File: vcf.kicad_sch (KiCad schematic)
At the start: 49 parts, among them J6 Conn_01x11_Pin, Q4 BC307, U19 Opamp_Dual, U24 LM13700, U25 LM13700

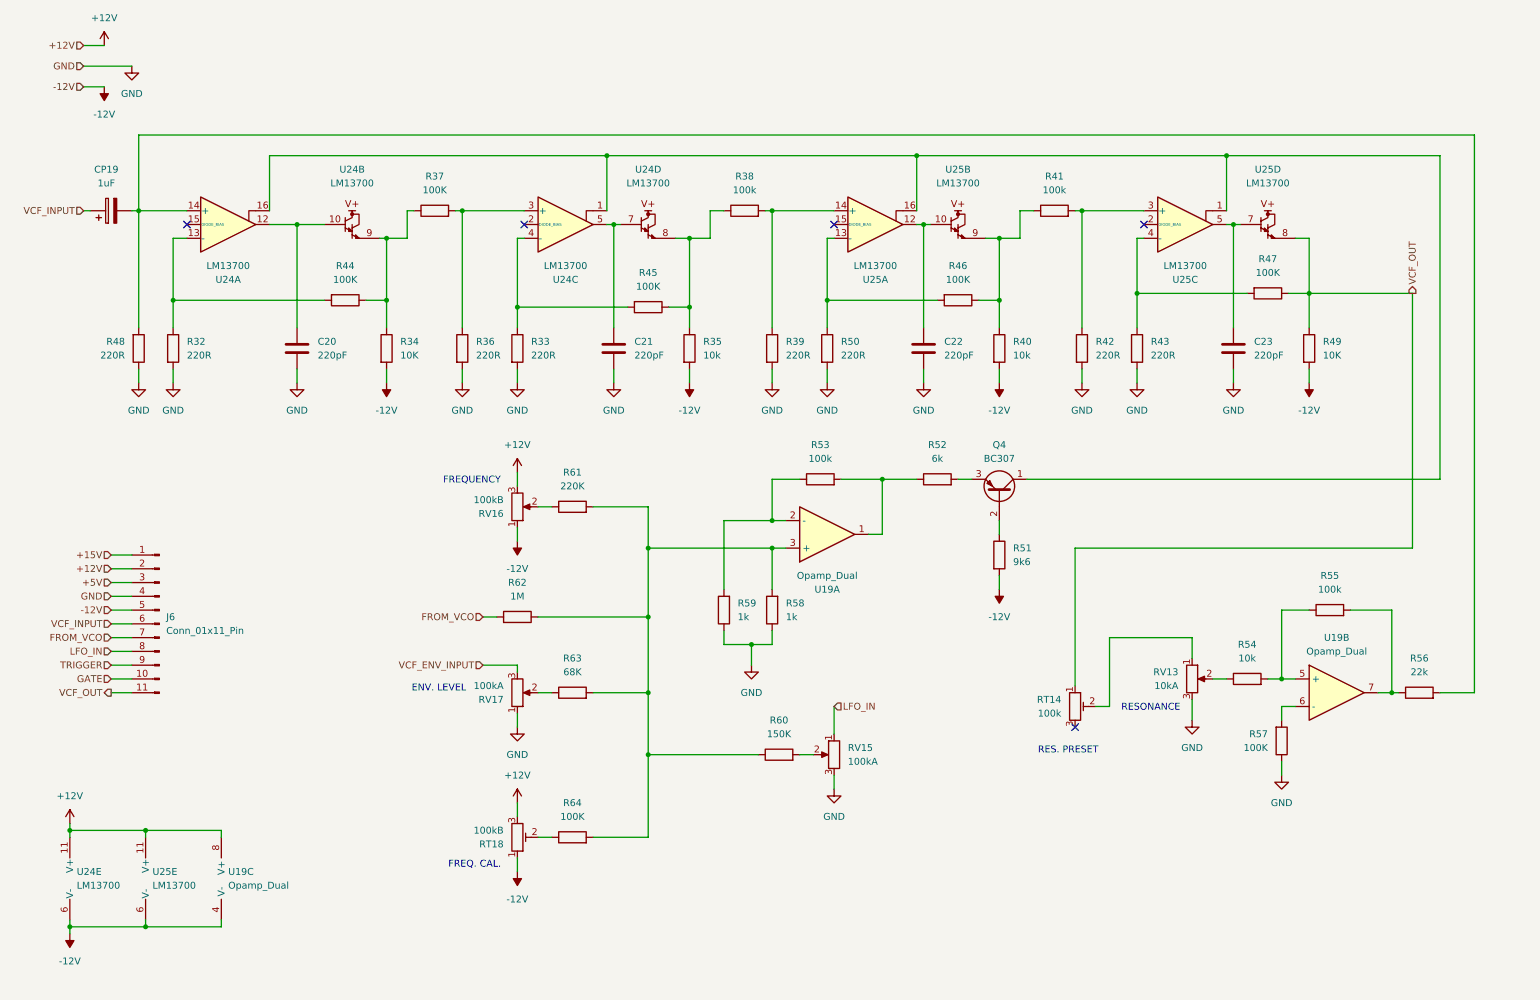
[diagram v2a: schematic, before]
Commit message: VCF components are in position (but PCB size is wrong)
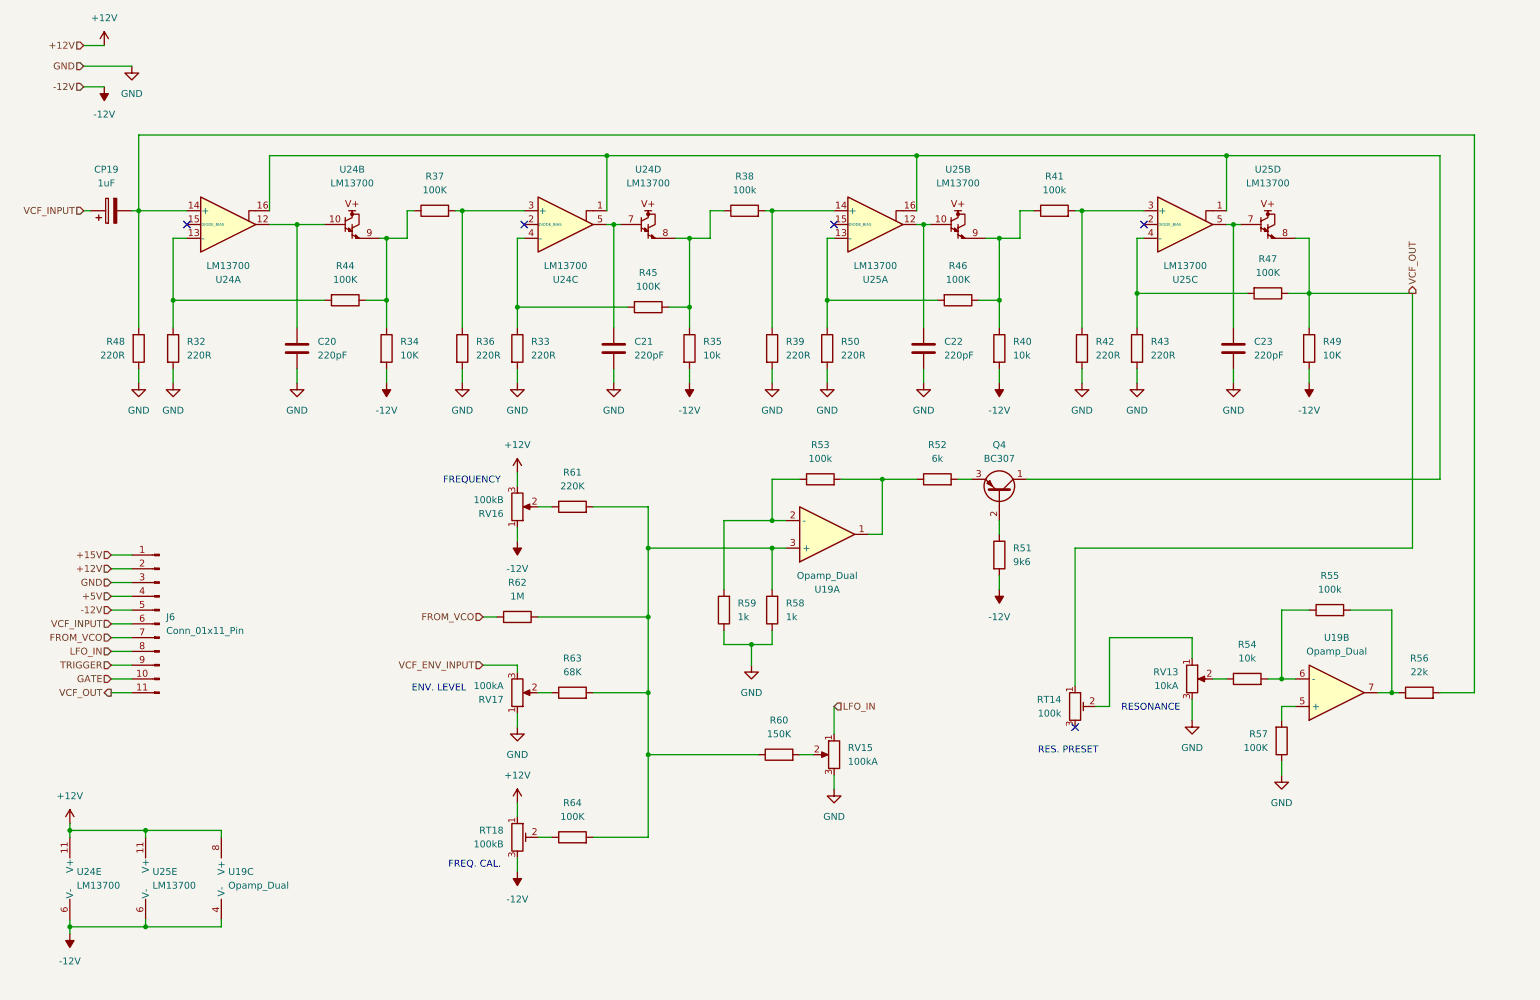
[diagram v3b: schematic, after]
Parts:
- Q4: footprint Package_TO_SOT_THT:TO-92_Inline -> Package_TO_SOT_THT:TO-92_Inline_Wide
- R32, R33, R34, R35, R36, R37, R38, R39, R40, R41, R42, R43, R44, R45, R46, R47, R48, R49, R50, R51, R52, R53, R54, R55, R56, R57, R58, R59, R60, R61, R62, R63, R64: footprint Resistor_THT:R_Axial_DIN0204_L3.6mm_D1.6mm_P7.62mm_Horizontal -> Resistor_THT:R_Axial_DIN0207_L6.3mm_D2.5mm_P15.24mm_Horizontal
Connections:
- net +12V: now also RT18.1; no longer RT18.3
- net +5V: now also J6.4 (Pin_4); no longer J6.3 (Pin_3)
- net -12V: now also RT18.3; no longer RT18.1
- net GND: now also J6.3 (Pin_3); no longer J6.4 (Pin_4)
- net at R54.2, R55.1: now also U19.6 (-); no longer U19.5 (+)
- net at R57.2: now also U19.5 (+); no longer U19.6 (-)
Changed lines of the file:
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@@
 	(hierarchical_label "GND"
 		(shape input)
-		(at 29.21 124.46 180)
+		(at 29.21 121.92 180)
 		(effects
 			(font
@@
 	(hierarchical_label "+5V"
 		(shape input)
-		(at 29.21 121.92 180)
+		(at 29.21 124.46 180)
 		(effects
 			(font
@@
 			)
 		)
-		(property "Footprint" "Resistor_THT:R_Axial_DIN0204_L3.6mm_D1.6mm_P7.62mm_Horizontal"
+		(property "Footprint" "Resistor_THT:R_Axial_DIN0207_L6.3mm_D2.5mm_P15.24mm_Horizontal"
 			(at 144.018 127 90)
 			(effects
@@
 			)
 		)
-		(property "Footprint" "Resistor_THT:R_Axial_DIN0204_L3.6mm_D1.6mm_P7.62mm_Horizontal"
+		(property "Footprint" "Resistor_THT:R_Axial_DIN0207_L6.3mm_D2.5mm_P15.24mm_Horizontal"
 			(at 72.39 68.072 90)
 			(effects
@@
 			)
 		)
-		(property "Footprint" "Resistor_THT:R_Axial_DIN0204_L3.6mm_D1.6mm_P7.62mm_Horizontal"
+		(property "Footprint" "Resistor_THT:R_Axial_DIN0207_L6.3mm_D2.5mm_P15.24mm_Horizontal"
 			(at 149.352 78.74 90)
 			(effects
@@
 			)
 		)
-		(property "Footprint" "Resistor_THT:R_Axial_DIN0204_L3.6mm_D1.6mm_P7.62mm_Horizontal"
+		(property "Footprint" "Resistor_THT:R_Axial_DIN0207_L6.3mm_D2.5mm_P15.24mm_Horizontal"
 			(at 102.362 78.74 90)
 			(effects
@@
 			)
 		)
-		(property "Footprint" "Resistor_THT:R_Axial_DIN0204_L3.6mm_D1.6mm_P7.62mm_Horizontal"
+		(property "Footprint" "Resistor_THT:R_Axial_DIN0207_L6.3mm_D2.5mm_P15.24mm_Horizontal"
 			(at 152.4 155.448 90)
 			(effects
@@
 			)
 		)
-		(property "Footprint" "Resistor_THT:R_Axial_DIN0204_L3.6mm_D1.6mm_P7.62mm_Horizontal"
+		(property "Footprint" "Resistor_THT:R_Axial_DIN0207_L6.3mm_D2.5mm_P15.24mm_Horizontal"
 			(at 32.512 78.74 90)
 			(effects
@@
 		(lib_id "Device:Opamp_Dual")
 		(at 255.27 142.24 0)
+		(mirror x)
 		(unit 2)
 		(exclude_from_sim no)
@@
 			)
 		)
-		(property "Footprint" "Resistor_THT:R_Axial_DIN0204_L3.6mm_D1.6mm_P7.62mm_Horizontal"
+		(property "Footprint" "Resistor_THT:R_Axial_DIN0207_L6.3mm_D2.5mm_P15.24mm_Horizontal"
 			(at 92.202 78.74 90)
 			(effects
@@
 			)
 		)
-		(property "Footprint" "Resistor_THT:R_Axial_DIN0204_L3.6mm_D1.6mm_P7.62mm_Horizontal"
+		(property "Footprint" "Resistor_THT:R_Axial_DIN0207_L6.3mm_D2.5mm_P15.24mm_Horizontal"
 			(at 191.262 116.84 90)
 			(effects
@@
 			)
 		)
-		(property "Footprint" "Resistor_THT:R_Axial_DIN0204_L3.6mm_D1.6mm_P7.62mm_Horizontal"
+		(property "Footprint" "Resistor_THT:R_Axial_DIN0207_L6.3mm_D2.5mm_P15.24mm_Horizontal"
 			(at 38.862 78.74 90)
 			(effects
@@
 		(lib_id "Device:R_Potentiometer_Trim")
 		(at 104.14 168.91 0)
-		(mirror x)
 		(unit 1)
 		(exclude_from_sim no)
@@
 		(dnp no)
 		(property "Reference" "RT18"
-			(at 101.6 170.1801 0)
+			(at 101.6 167.6399 0)
 			(effects
 				(font
@@
 		)
 		(property "Value" "100kB"
-			(at 101.6 167.6401 0)
+			(at 101.6 170.1799 0)
 			(effects
 				(font
@@
 			)
 		)
-		(property "Footprint" "Resistor_THT:R_Axial_DIN0204_L3.6mm_D1.6mm_P7.62mm_Horizontal"
+		(property "Footprint" "Resistor_THT:R_Axial_DIN0207_L6.3mm_D2.5mm_P15.24mm_Horizontal"
 			(at 114.3 170.688 90)
 			(effects
@@
 			)
 		)
-		(property "Footprint" "Resistor_THT:R_Axial_DIN0204_L3.6mm_D1.6mm_P7.62mm_Horizontal"
+		(property "Footprint" "Resistor_THT:R_Axial_DIN0207_L6.3mm_D2.5mm_P15.24mm_Horizontal"
 			(at 243.332 151.13 90)
 			(effects
@@
 			)
 		)
-		(property "Footprint" "Resistor_THT:R_Axial_DIN0204_L3.6mm_D1.6mm_P7.62mm_Horizontal"
+		(property "Footprint" "Resistor_THT:R_Axial_DIN0207_L6.3mm_D2.5mm_P15.24mm_Horizontal"
 			(at 160.02 104.648 90)
 			(effects
@@
 			)
 		)
-		(property "Footprint" "Resistor_THT:R_Axial_DIN0204_L3.6mm_D1.6mm_P7.62mm_Horizontal"
+		(property "Footprint" "Resistor_THT:R_Axial_DIN0207_L6.3mm_D2.5mm_P15.24mm_Horizontal"
 			(at 248.412 78.74 90)
 			(effects
@@
 			)
 		)
-		(property "Footprint" "Resistor_THT:R_Axial_DIN0204_L3.6mm_D1.6mm_P7.62mm_Horizontal"
+		(property "Footprint" "Resistor_THT:R_Axial_DIN0207_L6.3mm_D2.5mm_P15.24mm_Horizontal"
 			(at 206.502 78.74 90)
 			(effects
@@
 			)
 		)
-		(property "Footprint" "Resistor_THT:R_Axial_DIN0204_L3.6mm_D1.6mm_P7.62mm_Horizontal"
+		(property "Footprint" "Resistor_THT:R_Axial_DIN0207_L6.3mm_D2.5mm_P15.24mm_Horizontal"
 			(at 78.232 78.74 90)
 			(effects
@@
 			)
 		)
-		(property "Footprint" "Resistor_THT:R_Axial_DIN0204_L3.6mm_D1.6mm_P7.62mm_Horizontal"
+		(property "Footprint" "Resistor_THT:R_Axial_DIN0207_L6.3mm_D2.5mm_P15.24mm_Horizontal"
 			(at 146.05 55.118 90)
 			(effects
@@
 			)
 		)
-		(property "Footprint" "Resistor_THT:R_Axial_DIN0204_L3.6mm_D1.6mm_P7.62mm_Horizontal"
+		(property "Footprint" "Resistor_THT:R_Axial_DIN0207_L6.3mm_D2.5mm_P15.24mm_Horizontal"
 			(at 104.14 130.048 90)
 			(effects
@@
 			)
 		)
-		(property "Footprint" "Resistor_THT:R_Axial_DIN0204_L3.6mm_D1.6mm_P7.62mm_Horizontal"
+		(property "Footprint" "Resistor_THT:R_Axial_DIN0207_L6.3mm_D2.5mm_P15.24mm_Horizontal"
 			(at 185.42 68.072 90)
 			(effects
@@
 			)
 		)
-		(property "Footprint" "Resistor_THT:R_Axial_DIN0204_L3.6mm_D1.6mm_P7.62mm_Horizontal"
+		(property "Footprint" "Resistor_THT:R_Axial_DIN0207_L6.3mm_D2.5mm_P15.24mm_Horizontal"
 			(at 128.27 69.342 90)
 			(effects
@@
 			)
 		)
-		(property "Footprint" "Resistor_THT:R_Axial_DIN0204_L3.6mm_D1.6mm_P7.62mm_Horizontal"
+		(property "Footprint" "Resistor_THT:R_Axial_DIN0207_L6.3mm_D2.5mm_P15.24mm_Horizontal"
 			(at 270.51 144.018 90)
 			(effects
@@
 			)
 		)
-		(property "Footprint" "Resistor_THT:R_Axial_DIN0204_L3.6mm_D1.6mm_P7.62mm_Horizontal"
+		(property "Footprint" "Resistor_THT:R_Axial_DIN0207_L6.3mm_D2.5mm_P15.24mm_Horizontal"
 			(at 181.61 104.648 90)
 			(effects
@@
 			)
 		)
-		(property "Footprint" "Resistor_THT:R_Axial_DIN0204_L3.6mm_D1.6mm_P7.62mm_Horizontal"
+		(property "Footprint" "Resistor_THT:R_Axial_DIN0207_L6.3mm_D2.5mm_P15.24mm_Horizontal"
 			(at 242.57 66.802 90)
 			(effects
@@
 			)
 		)
-		(property "Footprint" "Resistor_THT:R_Axial_DIN0204_L3.6mm_D1.6mm_P7.62mm_Horizontal"
+		(property "Footprint" "Resistor_THT:R_Axial_DIN0207_L6.3mm_D2.5mm_P15.24mm_Horizontal"
 			(at 254 128.778 90)
 			(effects
@@
 			)
 		)
-		(property "Footprint" "Resistor_THT:R_Axial_DIN0204_L3.6mm_D1.6mm_P7.62mm_Horizontal"
+		(property "Footprint" "Resistor_THT:R_Axial_DIN0207_L6.3mm_D2.5mm_P15.24mm_Horizontal"
 			(at 216.662 78.74 90)
 			(effects
@@
 			)
 		)
-		(property "Footprint" "Resistor_THT:R_Axial_DIN0204_L3.6mm_D1.6mm_P7.62mm_Horizontal"
+		(property "Footprint" "Resistor_THT:R_Axial_DIN0207_L6.3mm_D2.5mm_P15.24mm_Horizontal"
 			(at 114.3 109.728 90)
 			(effects
@@
 			)
 		)
-		(property "Footprint" "Package_TO_SOT_THT:TO-92_Inline"
+		(property "Footprint" "Package_TO_SOT_THT:TO-92_Inline_Wide"
 			(at 191.135 100.33 0)
 			(effects
@@
 			)
 		)
-		(property "Footprint" "Resistor_THT:R_Axial_DIN0204_L3.6mm_D1.6mm_P7.62mm_Horizontal"
+		(property "Footprint" "Resistor_THT:R_Axial_DIN0207_L6.3mm_D2.5mm_P15.24mm_Horizontal"
 			(at 152.908 127 90)
 			(effects
@@
 			)
 		)
-		(property "Footprint" "Resistor_THT:R_Axial_DIN0204_L3.6mm_D1.6mm_P7.62mm_Horizontal"
+		(property "Footprint" "Resistor_THT:R_Axial_DIN0207_L6.3mm_D2.5mm_P15.24mm_Horizontal"
 			(at 114.3 144.018 90)
 			(effects
@@
 			)
 		)
-		(property "Footprint" "Resistor_THT:R_Axial_DIN0204_L3.6mm_D1.6mm_P7.62mm_Horizontal"
+		(property "Footprint" "Resistor_THT:R_Axial_DIN0207_L6.3mm_D2.5mm_P15.24mm_Horizontal"
 			(at 203.2 55.118 90)
 			(effects
@@
 			)
 		)
-		(property "Footprint" "Resistor_THT:R_Axial_DIN0204_L3.6mm_D1.6mm_P7.62mm_Horizontal"
+		(property "Footprint" "Resistor_THT:R_Axial_DIN0207_L6.3mm_D2.5mm_P15.24mm_Horizontal"
 			(at 238.76 141.478 90)
 			(effects
@@
 			)
 		)
-		(property "Footprint" "Resistor_THT:R_Axial_DIN0204_L3.6mm_D1.6mm_P7.62mm_Horizontal"
+		(property "Footprint" "Resistor_THT:R_Axial_DIN0207_L6.3mm_D2.5mm_P15.24mm_Horizontal"
 			(at 159.512 78.74 90)
 			(effects
@@
 			)
 		)
-		(property "Footprint" "Resistor_THT:R_Axial_DIN0204_L3.6mm_D1.6mm_P7.62mm_Horizontal"
+		(property "Footprint" "Resistor_THT:R_Axial_DIN0207_L6.3mm_D2.5mm_P15.24mm_Horizontal"
 			(at 134.112 78.74 90)
 			(effects
@@
 			)
 		)
-		(property "Footprint" "Resistor_THT:R_Axial_DIN0204_L3.6mm_D1.6mm_P7.62mm_Horizontal"
+		(property "Footprint" "Resistor_THT:R_Axial_DIN0207_L6.3mm_D2.5mm_P15.24mm_Horizontal"
 			(at 191.262 78.74 90)
 			(effects
@@
 			)
 		)
-		(property "Footprint" "Resistor_THT:R_Axial_DIN0204_L3.6mm_D1.6mm_P7.62mm_Horizontal"
+		(property "Footprint" "Resistor_THT:R_Axial_DIN0207_L6.3mm_D2.5mm_P15.24mm_Horizontal"
 			(at 88.9 55.118 90)
 			(effects

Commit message: Fix PCB sizes, adjust layout to new size
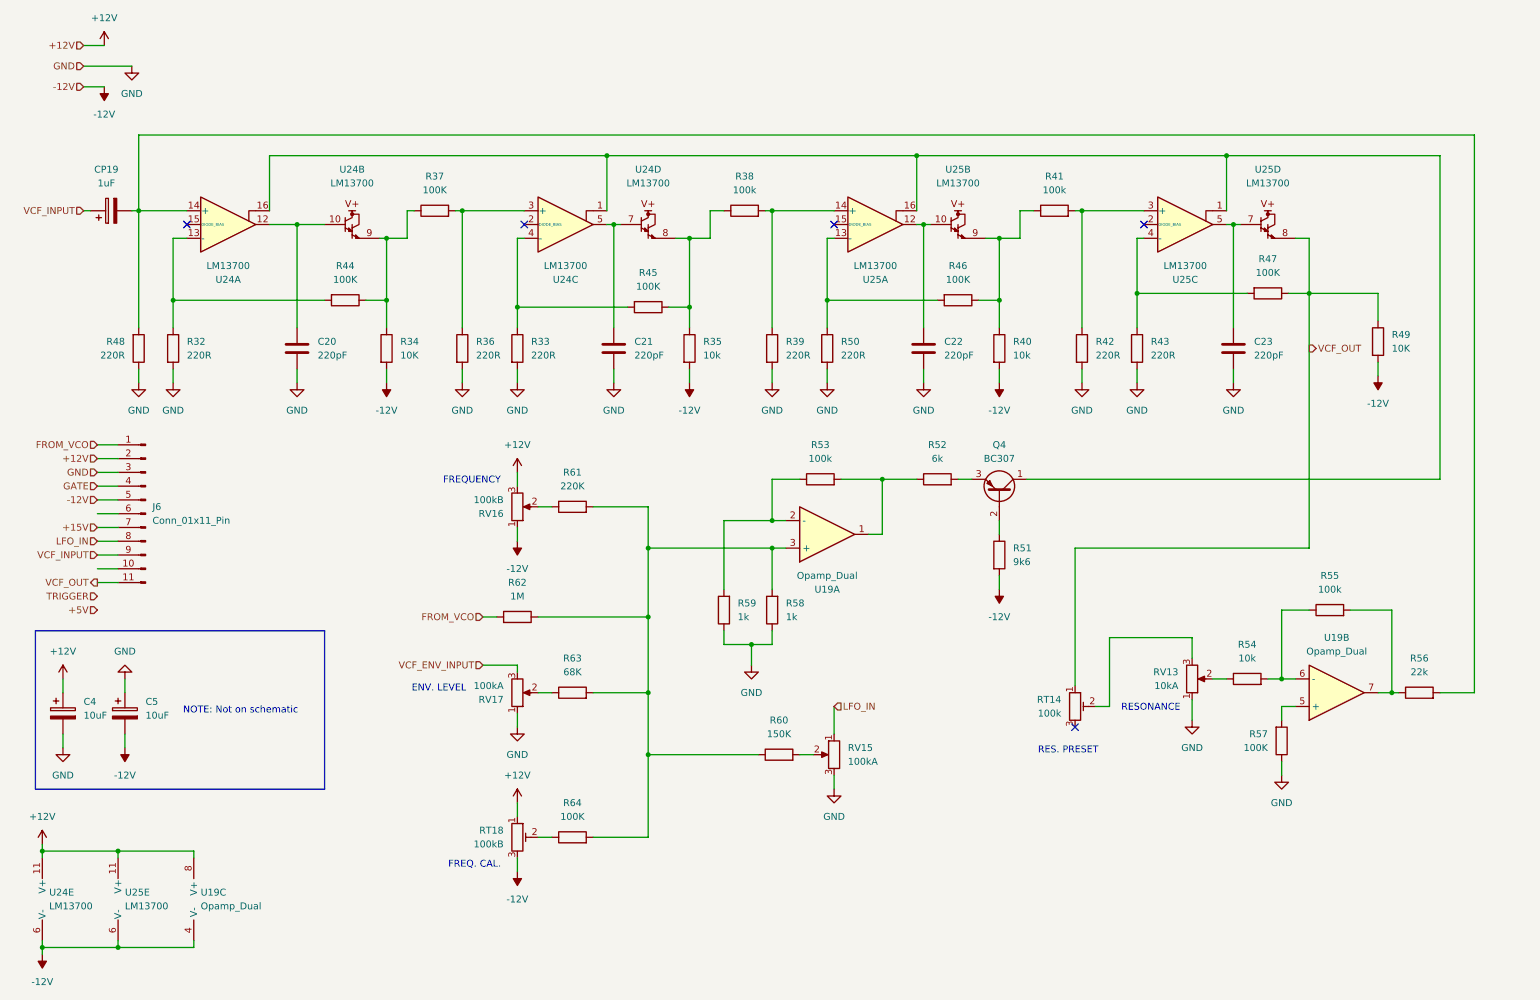
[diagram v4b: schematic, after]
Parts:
- added C4, C5: 10uF, Capacitor_THT:CP_Radial_D8.0mm_P3.80mm, symbol Device:C_Polarized
- CP19: footprint Capacitor_THT:CP_Radial_D8.0mm_P3.80mm -> Capacitor_THT:CP_Axial_L10.0mm_D4.5mm_P15.00mm_Horizontal
- RT14, RT18: footprint Potentiometer_THT:Potentiometer_Bourns_3339P_Vertical_HandSoldering -> Potentiometer_THT:Potentiometer_Piher_PT-10-V10_Vertical
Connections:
- net +12V: now also C4.1
- net +15V: now also J6.7 (Pin_7); no longer J6.1 (Pin_1)
- net +5V: no longer J6.4 (Pin_4)
- net -12V: now also C5.2
- net FROM_VCO: now also J6.1 (Pin_1); no longer J6.7 (Pin_7)
- net GATE: now also J6.4 (Pin_4); no longer J6.10 (Pin_10)
- net GND: now also RV13.1, C4.2, C5.1; no longer RV13.3
- net TRIGGER: no longer J6.9 (Pin_9)
- net VCF_INPUT: now also J6.9 (Pin_9); no longer J6.6 (Pin_6)
- net at RT14.2: now also RV13.3; no longer RV13.1
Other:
- note added: "NOTE: Not on schematic"
- moved on the sheet: J6, R49, U19C, U24E, U25E
